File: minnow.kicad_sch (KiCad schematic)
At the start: 66 parts, among them J3 PicoBlade, J3 USB_C_Receptacle_Host, J4 ARM_JTAG_SWD_10_Male, J4 VCCIO_EXT, P1 USB_C_Plug, SW1 SW_DIP_x04, U1 FT230XQ, U2 PI5A3157CEX, U3 PI5A3157CEX, U4 USB3740B-AI2, U5 SiP32432DR3

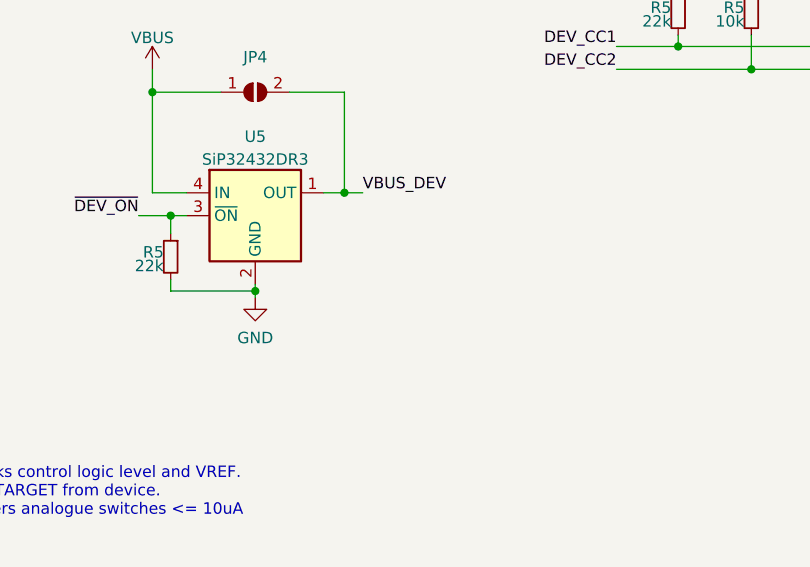
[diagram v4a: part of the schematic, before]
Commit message: add a white LED for VBUS_DEV
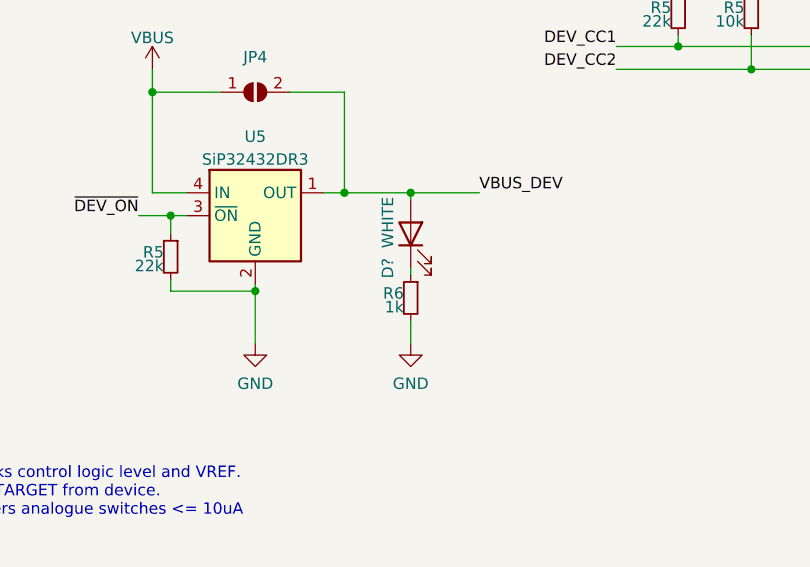
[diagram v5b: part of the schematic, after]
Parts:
- added D?: WHITE, LED_SMD:LED_0603_1608Metric, symbol Device:LED
- added R6: 1k, Resistor_SMD:R_0603_1608Metric, symbol Device:R_Small
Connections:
- net GND: now also R6.2
- net VBUS_DEV: now also D?.2 (A)
- new net: D?.1 (K), R6.1
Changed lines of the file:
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@@
   (title_block
     (title "Minnow - USB-C DAM Tool")
-    (date "2023-06-22")
-    (rev "2")
+    (date "2023-07-31")
+    (rev "3")
     (company "JBR Engineering Research Ltd")
     (comment 1 "J.Whittington 2023")
@@
   (junction (at 210.82 232.918) (diameter 0) (color 0 0 0 0)
   )
+  (junction (at 295.656 59.69) (diameter 0) (color 0 0 0 0)
+  )
   (junction (at 76.454 217.424) (diameter 0) (color 0 0 0 0)
   )
@@
     (stroke (width 0) (type default))
   )
-  (wire (pts (xy 278.384 70.612) (xy 278.384 71.374))
+  (wire (pts (xy 278.384 70.612) (xy 278.384 76.454))
     (stroke (width 0) (type default))
   )
@@
     (stroke (width 0) (type default))
   )
-  (wire (pts (xy 290.322 59.69) (xy 288.29 59.69))
+  (wire (pts (xy 303.276 59.69) (xy 295.656 59.69))
     (stroke (width 0) (type default))
   )
@@
     (stroke (width 0) (type default))
   )
+  (wire (pts (xy 295.656 59.69) (xy 295.656 60.452))
+    (stroke (width 0) (type default))
+  )
   (wire (pts (xy 123.698 241.3) (xy 128.524 241.3))
     (stroke (width 0) (type default))
@@
     (stroke (width 0) (type default))
   )
+  (wire (pts (xy 295.656 59.69) (xy 288.29 59.69))
+    (stroke (width 0) (type default))
+  )
   (wire (pts (xy 123.698 241.3) (xy 123.698 246.126))
     (stroke (width 0) (type default))
@@
     (stroke (width 0) (type default))
   )
+  (wire (pts (xy 295.656 73.914) (xy 295.656 76.454))
+    (stroke (width 0) (type default))
+  )
   (wire (pts (xy 49.276 106.68) (xy 49.276 107.696))
     (stroke (width 0) (type default))
@@
     (stroke (width 0) (type default))
   )
+  (wire (pts (xy 295.656 68.072) (xy 295.656 68.834))
+    (stroke (width 0) (type default))
+  )
   (wire (pts (xy 121.92 40.64) (xy 121.92 44.45))
     (stroke (width 0) (type default))
@@
     (effects (font (size 1.27 1.27)) (justify right bottom))
   )
-  (label "VBUS_DEV" (at 290.322 59.69 0) (fields_autoplaced)
+  (label "VBUS_DEV" (at 303.276 59.69 0) (fields_autoplaced)
     (effects (font (size 1.27 1.27)) (justify left bottom))
   )
@@
     )
   )
+  (symbol (lib_id "Device:LED") (at 295.656 64.262 90) (unit 1)
+    (in_bom yes) (on_board yes) (dnp no)
+    (property "Reference" "D?" (at 293.116 68.072 0)
+      (effects (font (size 1.27 1.27)))
+    )
+    (property "Value" "WHITE" (at 293.116 62.992 0)
+      (effects (font (size 1.27 1.27)))
+    )
+    (property "Footprint" "LED_SMD:LED_0603_1608Metric" (at 295.656 64.262 0)
+      (effects (font (size 1.524 1.524)) hide)
+    )
+    (property "Datasheet" "https://optoelectronics.liteon.com/upload/download/DS22-2006-062/LTW-C191DS5.PDF" (at 295.656 64.262 0)
+      (effects (font (size 1.524 1.524)) hide)
+    )
+    (property "MFN" "Lite-On Inc." (at 295.656 64.262 0)
+      (effects (font (size 1.27 1.27)) hide)
+    )
+    (property "MPN" "LTW-C191DS5" (at 295.656 64.262 0)
+      (effects (font (size 1.27 1.27)) hide)
+    )
+    (property "Characteristics" "" (at 295.656 64.262 0)
+      (effects (font (size 1.27 1.27)) hide)
+    )
+    (property "Description" "White LED Indication - Discrete 2.93V 0603 (1608 Metric)" (at 295.656 64.262 0)
+      (effects (font (size 1.27 1.27)) hide)
+    )
+    (property "SKU" "160-2239-1-ND" (at 295.656 64.262 0)
+      (effects (font (size 1.27 1.27)) hide)
+    )
+    (property "Vendor" "Digikey" (at 295.656 64.262 0)
+      (effects (font (size 1.27 1.27)) hide)
+    )
+    (property "Notes" "" (at 295.656 64.262 0)
+      (effects (font (size 1.27 1.27)) hide)
+    )
+    (property "Config" "" (at 295.656 64.262 0)
+      (effects (font (size 1.27 1.27)) hide)
+    )
+    (pin "1")
+    (pin "2")
+    (instances
+      (project "test-rig"
+        (path "/a5179d31-b893-4a85-b7eb-3ae5fec0a06b/00000000-0000-0000-0000-00005e062bfc"
+          (reference "D?") (unit 1)
+        )
+        (path "/a5179d31-b893-4a85-b7eb-3ae5fec0a06b/00000000-0000-0000-0000-00005e2107b4/00000000-0000-0000-0000-00005e062bfc"
+          (reference "D?") (unit 1)
+        )
+        (path "/a5179d31-b893-4a85-b7eb-3ae5fec0a06b/00000000-0000-0000-0000-00005e5a3556"
+          (reference "D?") (unit 1)
+        )
+        (path "/a5179d31-b893-4a85-b7eb-3ae5fec0a06b/00000000-0000-0000-0000-0000614bf719"
+          (reference "D?") (unit 1)
+        )
+        (path "/a5179d31-b893-4a85-b7eb-3ae5fec0a06b"
+          (reference "D5") (unit 1)
+        )
+      )
+      (project "minnow"
+        (path "/bbabdafc-86d4-4010-b464-a3e83875bd6e"
+          (reference "D4") (unit 1)
+        )
+      )
+    )
+  )
   (symbol (lib_id "Device:C") (at 130.556 48.26 0) (unit 1)
     (in_bom yes) (on_board yes) (dnp no)
@@
     )
   )
+  (symbol (lib_id "Device:R_Small") (at 295.656 71.374 0) (mirror y) (unit 1)
+    (in_bom yes) (on_board yes) (dnp no)
+    (property "Reference" "R6" (at 294.894 70.866 0)
+      (effects (font (size 1.27 1.27)) (justify left))
+    )
+    (property "Value" "1k" (at 294.894 72.39 0)
+      (effects (font (size 1.27 1.27)) (justify left))
+    )
+    (property "Footprint" "Resistor_SMD:R_0603_1608Metric" (at 295.656 71.374 0)
+      (effects (font (size 1.27 1.27)) hide)
+    )
+    (property "Datasheet" "" (at 295.656 71.374 0)
+      (effects (font (size 1.27 1.27)) hide)
+    )
+    (property "Characteristics" "5%" (at 295.656 71.374 0)
+      (effects (font (size 1.27 1.27)) hide)
+    )
+    (property "Config" "" (at 295.656 71.374 0)
+      (effects (font (size 1.27 1.27)) hide)
+    )
+    (property "MFN" "" (at 295.656 71.374 0)
+      (effects (font (size 1.27 1.27)) hide)
+    )
+    (property "MPN" "" (at 295.656 71.374 0)
+      (effects (font (size 1.27 1.27)) hide)
+    )
+    (property "Description" "" (at 295.656 71.374 0)
+      (effects (font (size 1.27 1.27)) hide)
+    )
+    (property "Notes" "" (at 295.656 71.374 0)
+      (effects (font (size 1.27 1.27)) hide)
+    )
+    (property "Vendor" "" (at 295.656 71.374 0)
+      (effects (font (size 1.27 1.27)) hide)
+    )
+    (property "SKU" "" (at 295.656 71.374 0)
+      (effects (font (size 1.27 1.27)) hide)
+    )
+    (pin "1")
+    (pin "2")
+    (instances
+      (project "minnow"
+        (path "/aa74195b-ecf6-4690-a06f-906cb3a91665"
+          (reference "R6") (unit 1)
+        )
+      )
+      (project "minnow"
+        (path "/bbabdafc-86d4-4010-b464-a3e83875bd6e"
+          (reference "R16") (unit 1)
+        )
+      )
+    )
+  )
   (symbol (lib_id "Connector:TestPoint_Small") (at 180.848 57.15 0) (unit 1)
     (in_bom yes) (on_board yes) (dnp no) (fields_autoplaced)
@@
     )
   )
-  (symbol (lib_id "power:GND") (at 278.384 71.374 0) (unit 1)
+  (symbol (lib_id "power:GND") (at 278.384 76.454 0) (unit 1)
     (in_bom yes) (on_board yes) (dnp no) (fields_autoplaced)
-    (property "Reference" "#PWR037" (at 278.384 77.724 0)
+    (property "Reference" "#PWR037" (at 278.384 82.804 0)
       (effects (font (size 1.27 1.27)) hide)
     )
-    (property "Value" "GND" (at 278.384 75.8174 0)
+    (property "Value" "GND" (at 278.384 80.8974 0)
       (effects (font (size 1.27 1.27)))
     )
-    (property "Footprint" "" (at 278.384 71.374 0)
+    (property "Footprint" "" (at 278.384 76.454 0)
       (effects (font (size 1.27 1.27)) hide)
     )
-    (property "Datasheet" "" (at 278.384 71.374 0)
+    (property "Datasheet" "" (at 278.384 76.454 0)
       (effects (font (size 1.27 1.27)) hide)
     )
@@
         )
       )
+    )
+  )
+  (symbol (lib_id "power:GND") (at 295.656 76.454 0) (unit 1)
+    (in_bom yes) (on_board yes) (dnp no) (fields_autoplaced)
+    (property "Reference" "#PWR06" (at 295.656 82.804 0)
+      (effects (font (size 1.27 1.27)) hide)
+    )
+    (property "Value" "GND" (at 295.656 80.8974 0)
+      (effects (font (size 1.27 1.27)))
+    )
+    (property "Footprint" "" (at 295.656 76.454 0)
+      (effects (font (size 1.27 1.27)) hide)
+    )
+    (property "Datasheet" "" (at 295.656 76.454 0)
+      (effects (font (size 1.27 1.27)) hide)
+    )
+    (pin "1")
+    (instances
+      (project "minnow"
+        (path "/bbabdafc-86d4-4010-b464-a3e83875bd6e"
+          (reference "#PWR06") (unit 1)
+        )
+      )
+      (project "spirit_logger_hardware"
+        (path "/e63e39d7-6ac0-4ffd-8aa3-1841a4541b55/d2441721-f207-485a-a2ad-c09a5d6e4db8"
+          (reference "#PWR0140") (unit 1)
+        )
+      )

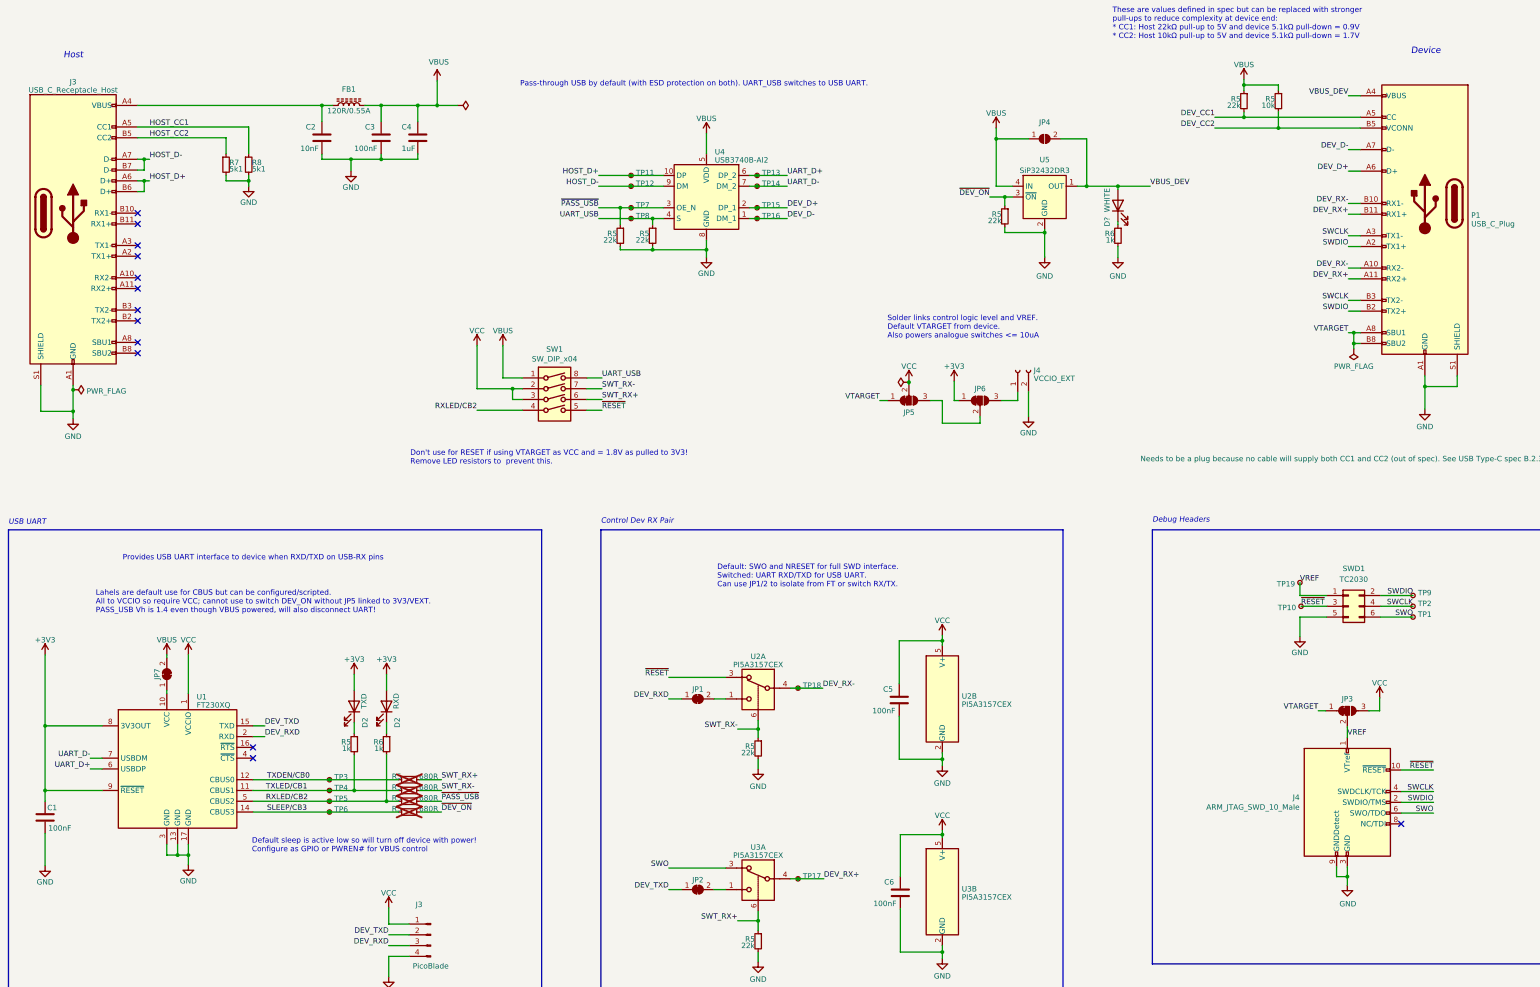
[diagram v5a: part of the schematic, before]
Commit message: migrate to KiCad 9.0
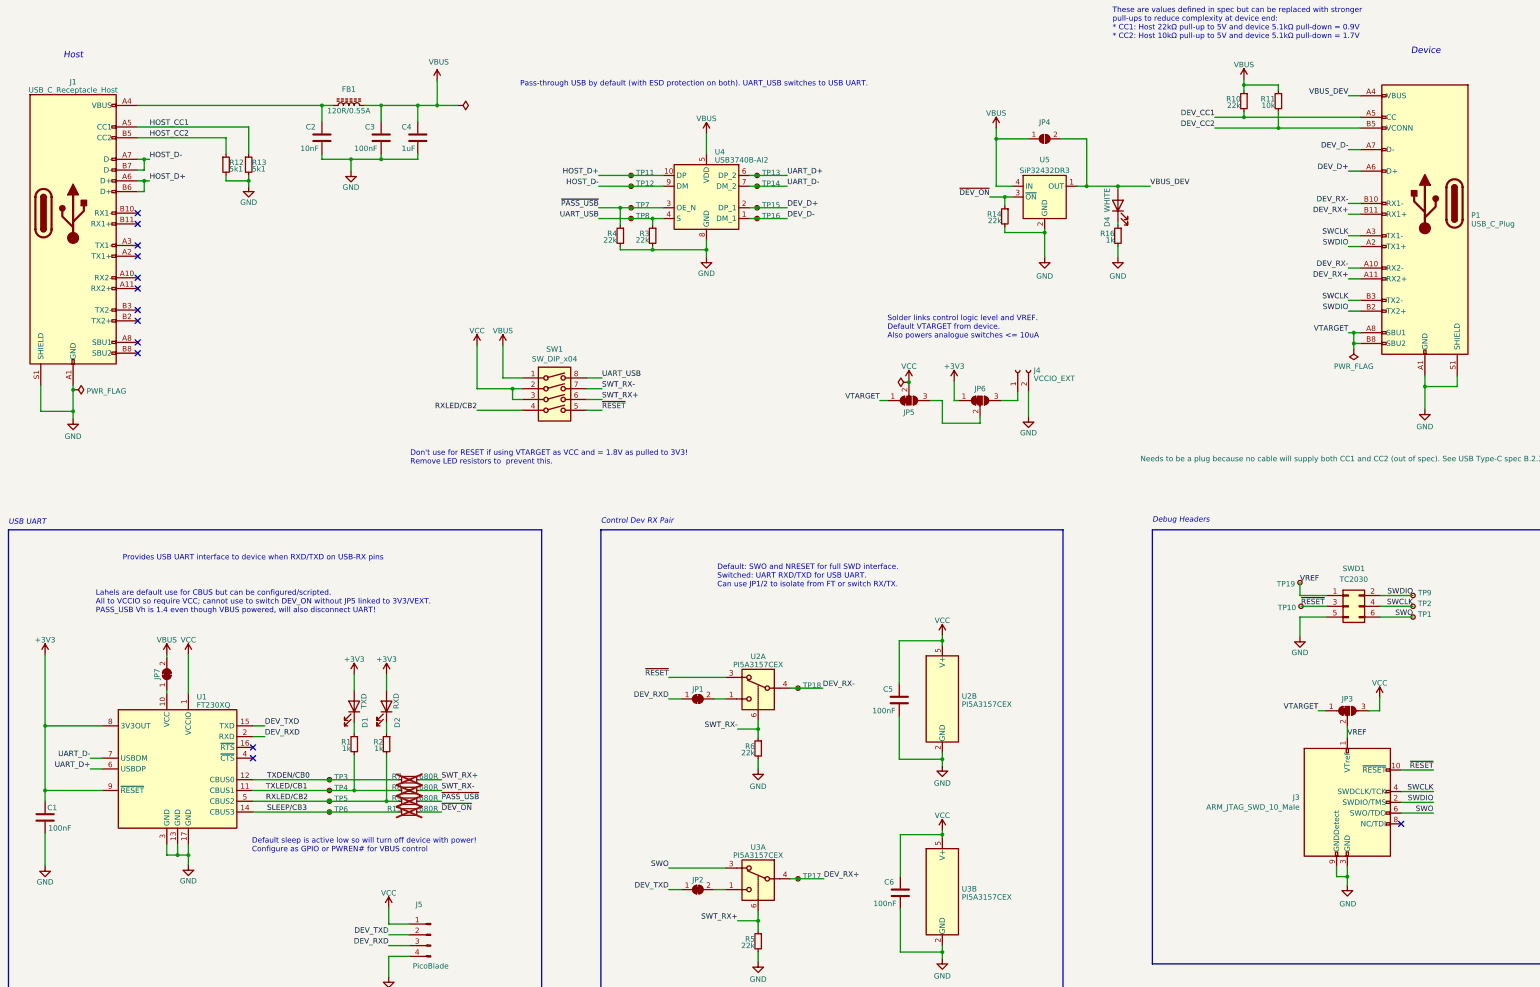
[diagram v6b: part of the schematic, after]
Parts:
- gave numbers to parts that had none: 1
- renumbered D2 to D1, J3 to J1, J4 to J3, J3 to J5, R5 to R1, R5 to R10, R5 to R11, R7 to R12, R8 to R13, R5 to R14, R5 to R15, R6 to R16, R6 to R2, R5 to R3, R5 to R4, R5 to R6, R5 to R7, R5 to R8, R5 to R9

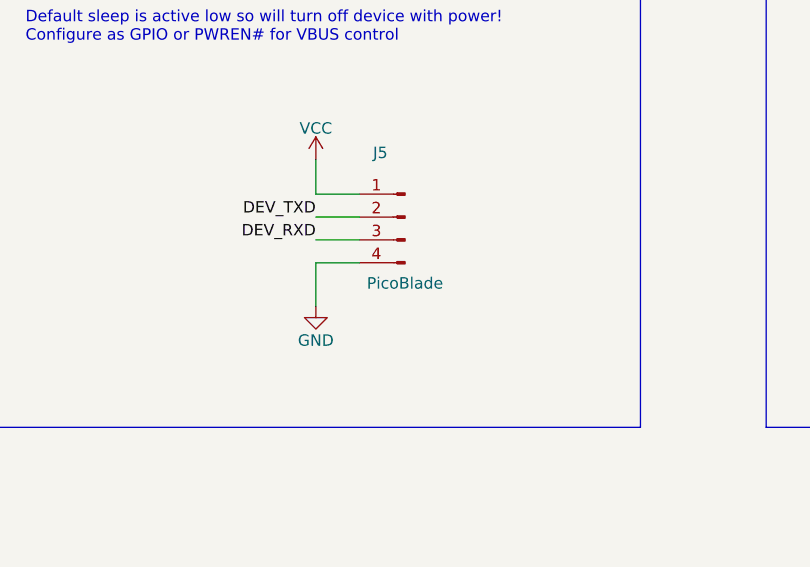
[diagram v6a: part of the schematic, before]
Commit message: add supplier jlcpcb and lcsc codes
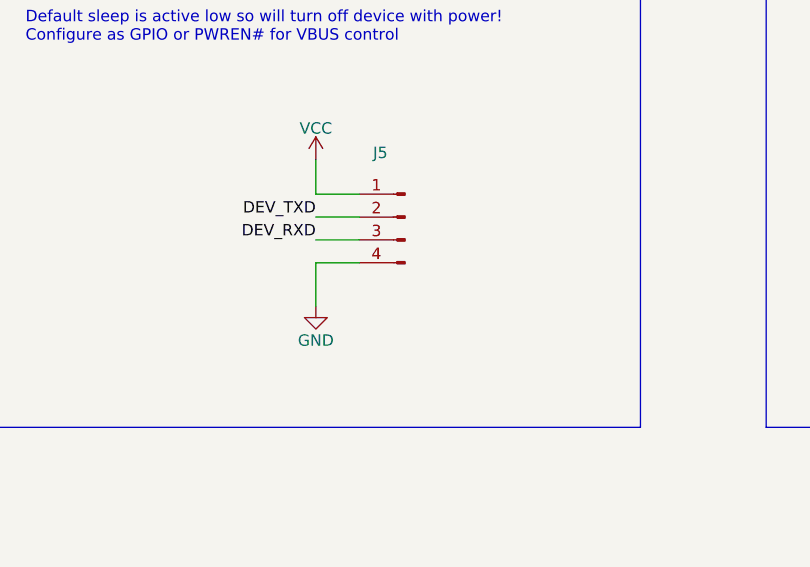
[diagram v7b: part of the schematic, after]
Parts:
- D1: LCSC (none) -> C5189028
- D2: LCSC (none) -> C5246833
- D4: LCSC (none) -> C575431
- FB1: LCSC (none) -> C14709
- J1: LCSC (none) -> C5119948
- J3: LCSC (none) -> C2972785
- J5: value PicoBlade -> ~; SKU WM7622CT-ND -> (none); Vendor Digikey -> (none)
- P1: LCSC (none) -> C134082
- SW1: LCSC (none) -> C3312308
- U1: LCSC (none) -> C128629
- U2, U3: LCSC (none) -> C41431789
- U4: LCSC (none) -> C626690
- U5: LCSC (none) -> C2149830
